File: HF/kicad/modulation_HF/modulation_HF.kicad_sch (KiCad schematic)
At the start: 44 parts, among them J1 Conn_01x05_Pin, J2 Screw_Terminal_01x02, J3 Conn_Coaxial, J4 Screw_Terminal_01x04, U2 ADE-6, U3 ADE-6, U5 74HCT00, U6 MASW-007221, U7 74HCT00, U8 LTC6268xS6-10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

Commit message: ajout carte adaptation pr antenne + comparateur pour sortie demodulation
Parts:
- added unit 5 of U5
- added unit 4 of U5
- renumbered U7 to U5
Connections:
- net +5V: now also U5.14 (VCC)
- net GND: now also U6.2 (GND), U5.7 (GND)
- net ctrl_Sortie_Antenne: now also U5.10, U5.9; no longer U5.1, U5.2
- net ~{ctrl_Sortie_Antenne}: now also U5.8; no longer U5.3
- no-connect marks 14 -> 17

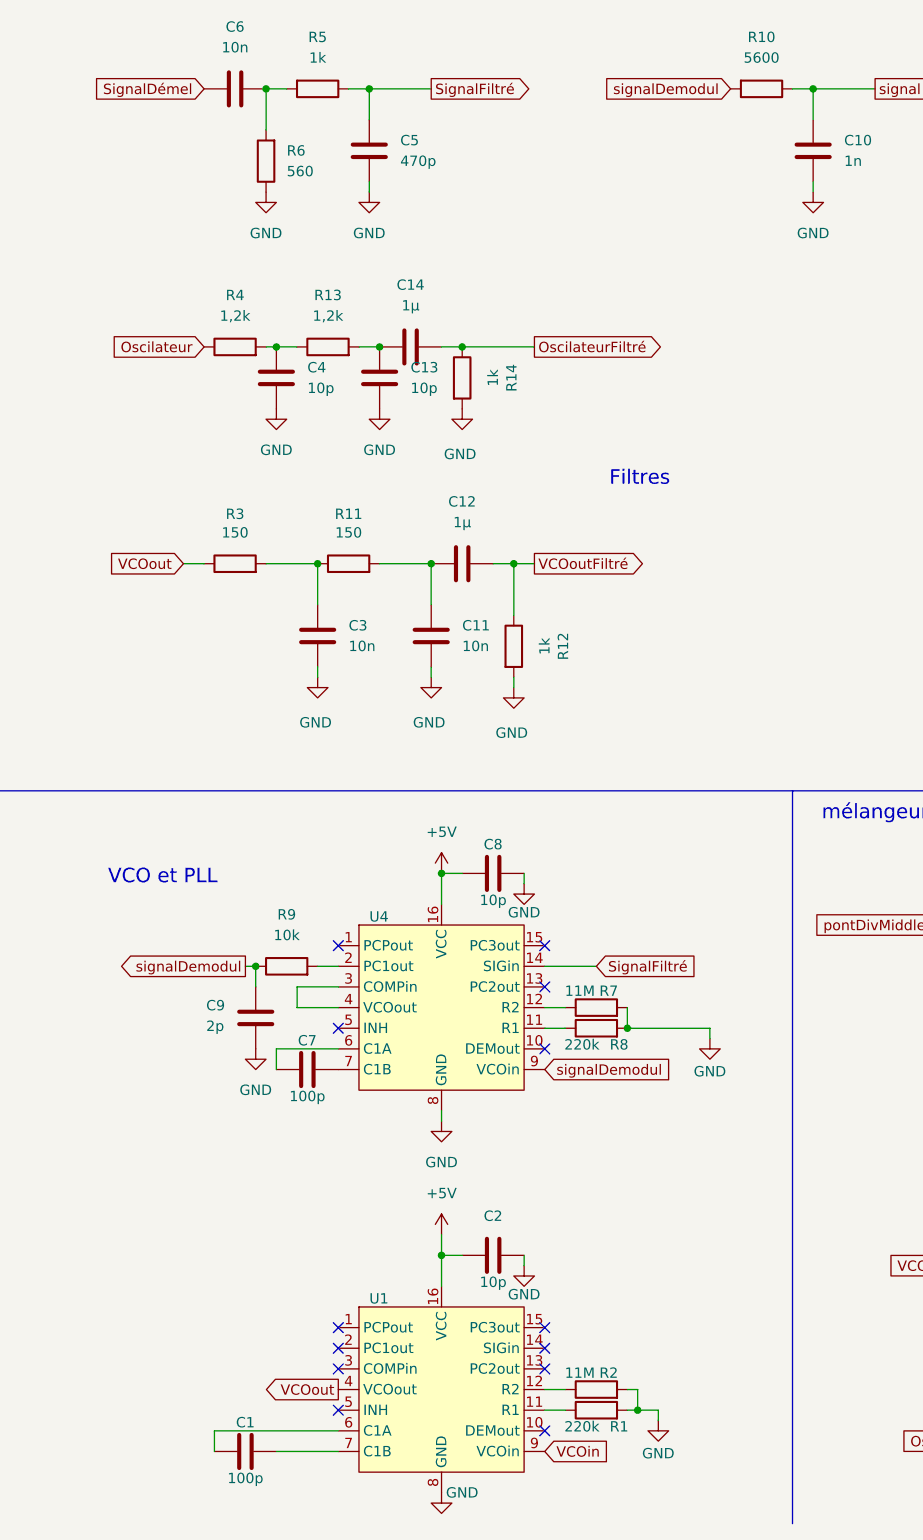
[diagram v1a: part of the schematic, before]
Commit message: modif kicad pour ajusté au test sur platin
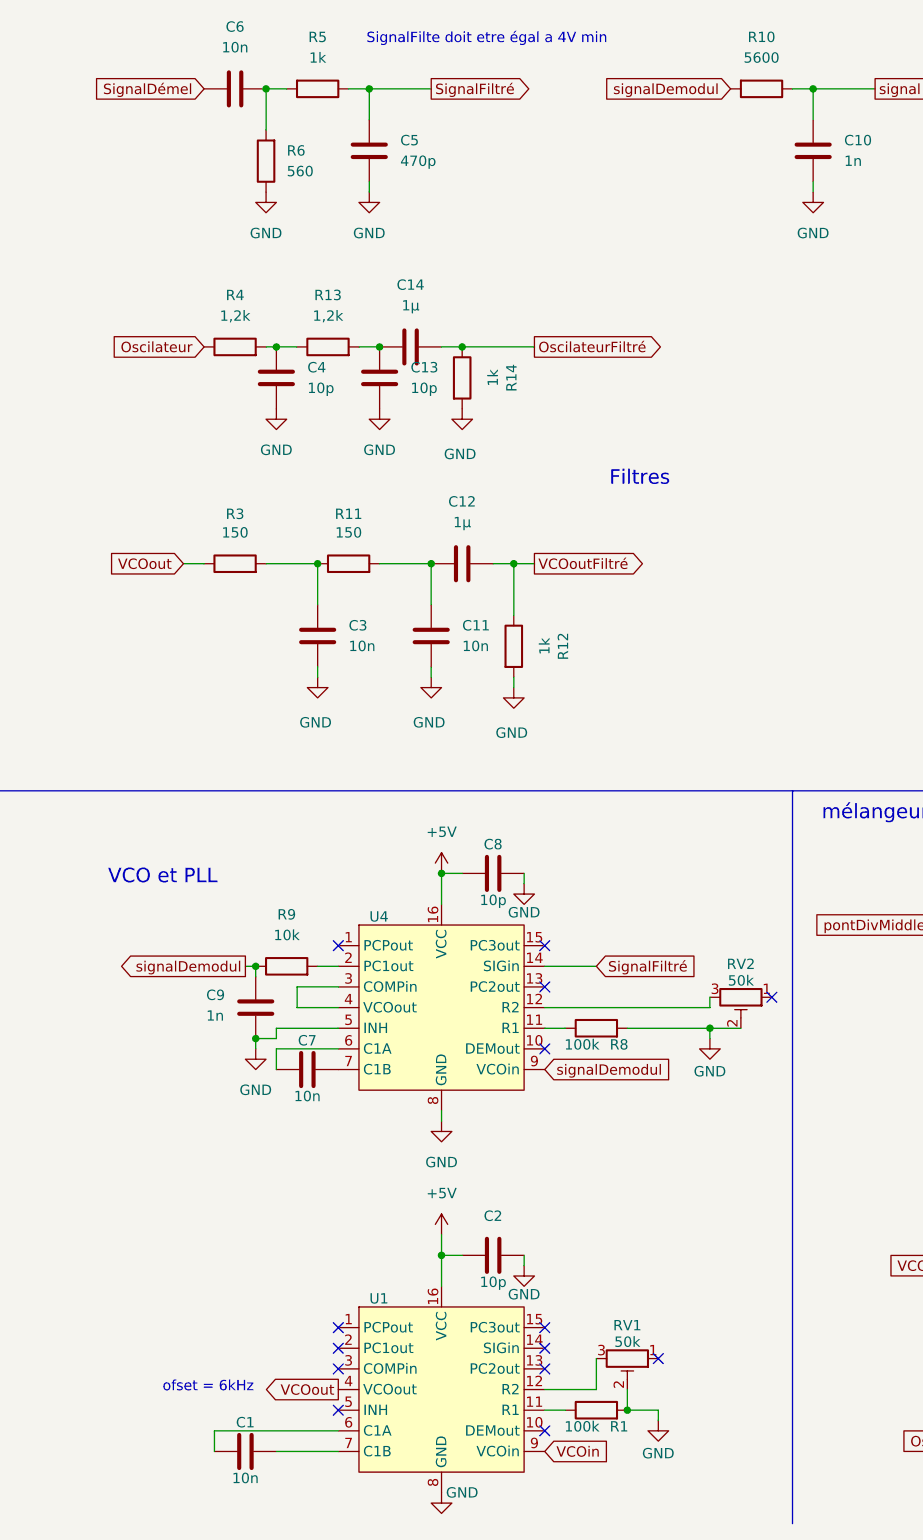
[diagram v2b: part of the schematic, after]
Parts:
- removed R2, R7: 11M, symbol Device:R
- added RV1, RV2: 50k, symbol Device:R_Potentiometer_Trim
- C1, C7: value 100p -> 10n
- C9: value 2p -> 1n
- R1, R8: value 220k -> 100k
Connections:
- net GND: now also U4.5 (INH), RV1.2, RV2.2
- net at U4.12 (R2): now also RV2.3
- net at U1.12 (R2): now also RV1.3
- no-connect marks 17 -> 18
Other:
- note added: "SignalFilte doit etre égal a 4V min"
- note added: "ofset = 6kHz"
- moved on the sheet: C9

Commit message: modification pour incorporer une image
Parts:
- R9: value 10k -> 1k
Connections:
- net GND: now also U1.5 (INH)
- no-connect marks 18 -> 17
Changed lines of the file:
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@@
 	)
 	(no_connect
-		(at 54.61 184.15)
-	)
-	(no_connect
 		(at 54.61 176.53)
 	)
@@
 	(wire
 		(pts
+			(xy 54.61 184.15) (xy 33.02 184.15)
+		)
+		(stroke
+			(width 0)
+			(type default)
+		)
+	)
+	(wire
+		(pts
 			(xy 100.33 137.16) (xy 100.33 138.43)
 		)
@@
 	(wire
 		(pts
+			(xy 33.02 184.15) (xy 33.02 185.42)
+		)
+		(stroke
+			(width 0)
+			(type default)
+		)
+	)
+	(wire
+		(pts
 			(xy 186.69 40.64) (xy 166.37 40.64)
 		)
@@
 	)
 	(symbol
+		(lib_id "power:GND")
+		(at 33.02 185.42 0)
+		(unit 1)
+		(exclude_from_sim no)
+		(in_bom yes)
+		(on_board yes)
+		(dnp no)
+		(fields_autoplaced yes)
+		(property "Reference" "#PWR031"
+			(at 33.02 191.77 0)
+			(effects
+				(font
+					(size 1.27 1.27)
+				)
+				(hide yes)
+			)
+		)
+		(property "Value" "GND"
+			(at 33.02 190.5 0)
+			(effects
+				(font
+					(size 1.27 1.27)
+				)
+			)
+		)
+		(property "Footprint" ""
+			(at 33.02 185.42 0)
+			(effects
+				(font
+					(size 1.27 1.27)
+				)
+				(hide yes)
+			)
+		)
+		(property "Datasheet" ""
+			(at 33.02 185.42 0)
+			(effects
+				(font
+					(size 1.27 1.27)
+				)
+				(hide yes)
+			)
+		)
+		(property "Description" "Power symbol creates a global label with name \"GND\" , ground"
+			(at 33.02 185.42 0)
+			(effects
+				(font
+					(size 1.27 1.27)
+				)
+				(hide yes)
+			)
+		)
+		(pin "1"
+		)
+		(instances
+			(project ""
+				(path "/946d0ff1-e2f0-4b2e-89d7-bc0f32795ea7"
+					(reference "#PWR031")
+					(unit 1)
+				)
+			)
+		)
+	)
+	(symbol
 		(lib_id "Device:R")
 		(at 86.36 137.16 90)
@@
 			)
 		)
-		(property "Value" "10k"
+		(property "Value" "1k"
 			(at 48.26 125.73 90)
 			(effects

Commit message: mise a jours schemas kicad
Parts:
- removed RV1, RV2: 50k, symbol Device:R_Potentiometer_Trim
- added C16: 10n, symbol Device:C
- added R17, R2: 47k, symbol Device:R
- added R7: 470, symbol Device:R
- C1: value 10n -> 100n
- C7: value 10n -> 100p
- R1, R8: value 100k -> 33k
- R9: value 1k -> 10k
- U1, U4: value ~ -> (none)
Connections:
- net GND: now also R17.1, R2.1
- net SignalFiltré: now also C16.1; no longer U4.14 (SIGin)
- net VCOin: now also R7.2; no longer U1.9 (VCOin)
- net at U1.12 (R2): now also R2.2
- net at U4.12 (R2): now also R17.2
- new net: C16.2, U4.14 (SIGin)
- new net: R7.1, U1.9 (VCOin)
- no-connect marks 17 -> 15
